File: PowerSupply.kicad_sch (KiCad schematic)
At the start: 0 parts

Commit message: PowerSupply start
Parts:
- added C7, C8: 47uF 450V, symbol Device:C_Polarized_US
- added D3, D4, D5, D6: UF4007, Diode_THT:D_DO-41_SOD81_P10.16mm_Horizontal, symbol Diode:1N4007
- added L1: 4H, symbol Device:L
- added R18: 470K 1W, symbol Device:R_US
- added R19: R_US, symbol Device:R_US
- added SW1: Standby, symbol Switch:SW_SPST
- added TR2: Hammond_269AAX, symbol Transformer_Audio:Hammond_269AAX
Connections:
- new net: C7.1, D5.1 (K), D6.1 (K), R18.1, SW1.1 (A)
- new net: D3.1 (K), D6.2 (A), TR2.4 (RED)
- new net: C8.1, L1.2, R19.1
- new net: C7.2, C8.2, D3.2 (A), D4.2 (A), R18.2
- new net: D4.1 (K), D5.2 (A)
- new net B+OPT: L1.1, SW1.2 (B)
- new net B+PI: R19.2
- new net Fil1: TR2.7 (GRN/YEL)
- new net Fil2: TR2.9 (GRN)
- no-connect marks 0 -> 1

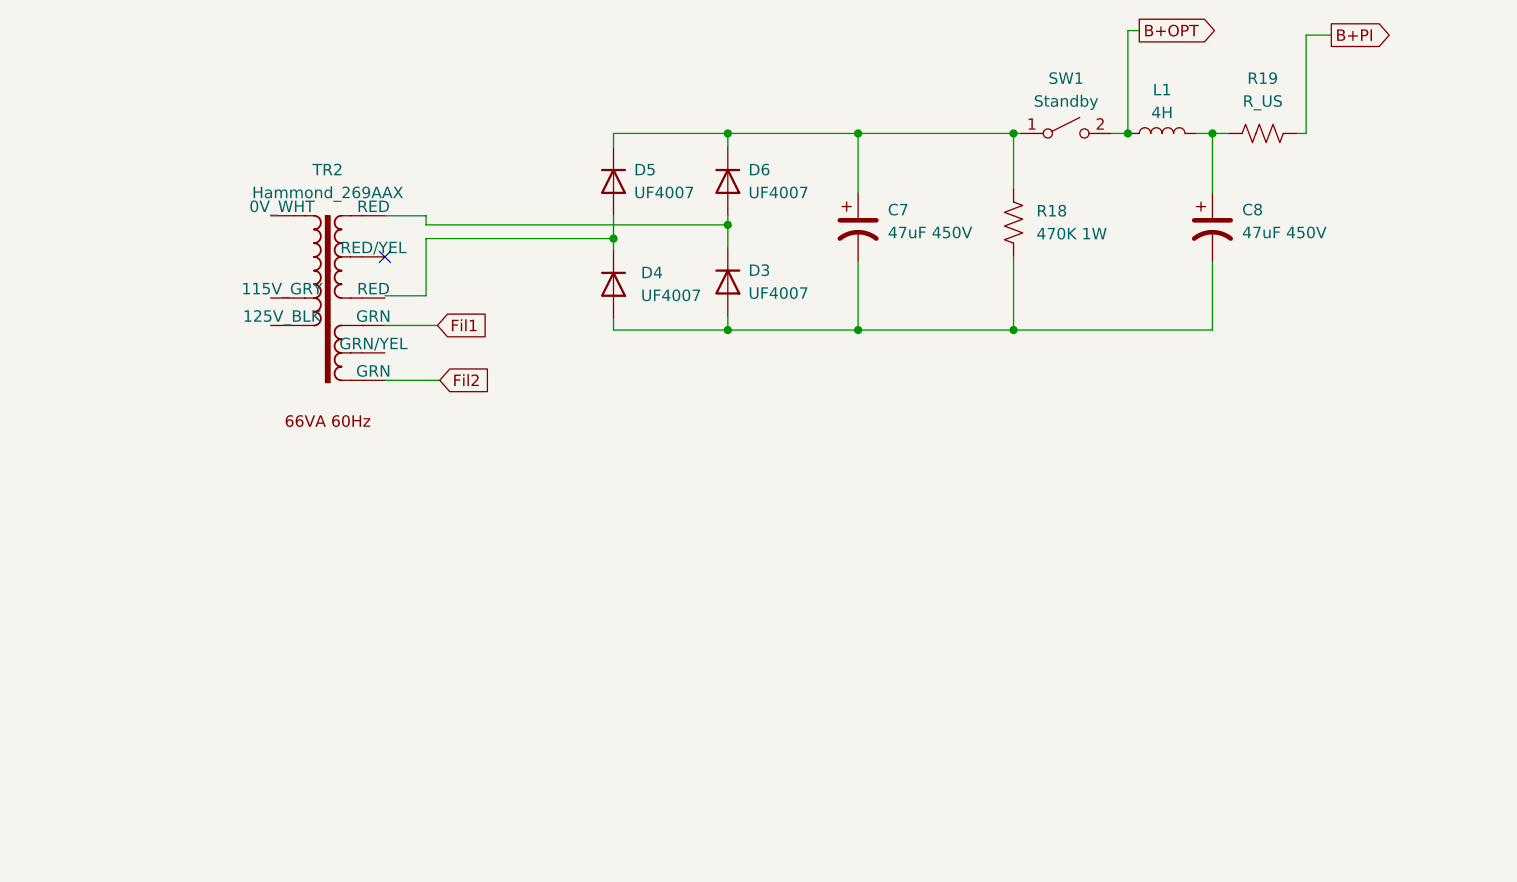
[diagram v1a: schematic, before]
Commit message: Add Rectifier PCB
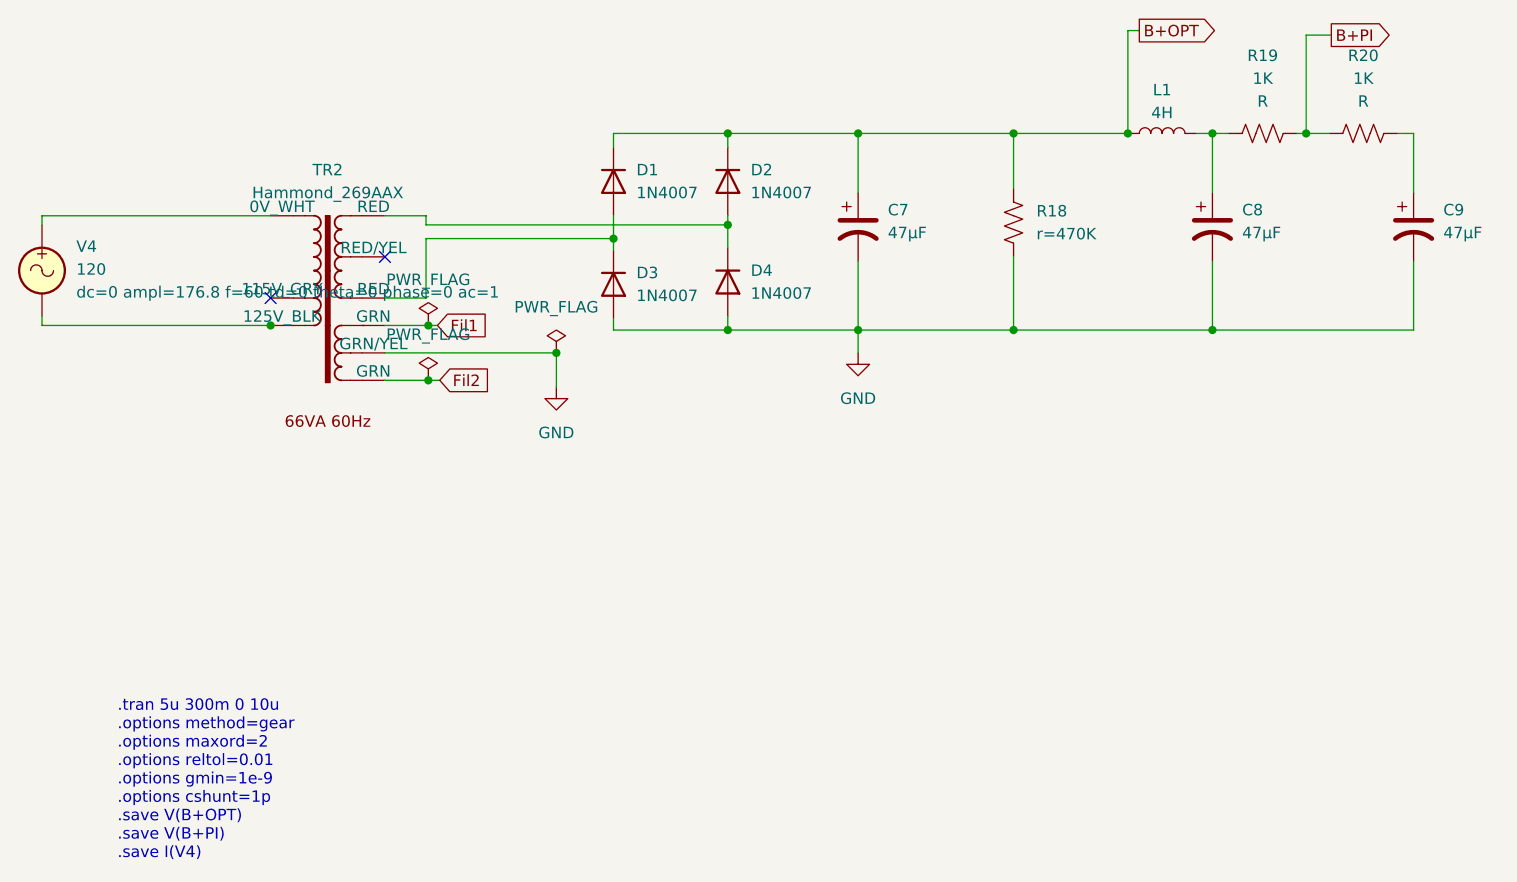
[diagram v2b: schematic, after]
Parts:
- removed D5, D6: UF4007, Diode_THT:D_DO-41_SOD81_P10.16mm_Horizontal, symbol Diode:1N4007
- removed SW1: Standby, symbol Switch:SW_SPST
- added C9: 47µF, symbol Device:C_Polarized_US
- added D1, D2: 1N4007, Diode_THT:D_DO-41_SOD81_P10.16mm_Horizontal, symbol Diode:1N4007
- added R20: 1K, symbol Device:R_US
- added V4: 120, symbol Simulation_SPICE:VSIN
- C7, C8: value 47uF 450V -> 47µF
- D3, D4: value UF4007 -> 1N4007
- R18: value 470K 1W -> ${SIM.PARAMS}
- R19: value R_US -> 1K
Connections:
- net B+OPT: now also C7.1, R18.1, D1.1 (K), D2.1 (K)
- net B+PI: now also R20.1
- net at TR2.4 (RED): now also D4.1 (K), D2.2 (A); no longer D3.1 (K)
- net at C7.2, C8.2, D3.2 (A)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: now also C9.2
- net at TR2.1 (0V_WHT): now also V4.1
- net at TR2.3 (125V_BLK): now also V4.2
- net at TR2.6 (RED): now also D3.1 (K), D1.2 (A)
- new net: C9.1, R20.2
- new net GND: TR2.8 (GRN/YEL)
- no-connect marks 1 -> 2
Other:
- note added: ".tran 5u 300m 0 10u .options method=gear .options maxord=2 .options reltol=0.01 .options gmin=1e-9 .options cshunt=1p .save V(B+OPT) .save V(B+PI) .save I(V4)"
